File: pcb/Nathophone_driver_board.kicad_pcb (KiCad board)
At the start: 4 copper layers, 160 x 110 mm, 223 parts, among them J1 PJ-063AH, J10 TERM BLOCK, J11 54202-S0806ALF, J12 54202-S0806ALF, J13 54202-S0806ALF, J14 54202-S0806ALF, J3 Conn_01x30, J4 54202-S0806ALF, J5 TERM BLOCK, J6 TERM BLOCK, J7 TERM BLOCK, J8 TERM BLOCK, J9 TERM BLOCK, Q1 2N7002H, Q10 BSS84, Q11 BSS84, Q12 2N7002H, Q13 2N7002H, Q2 2N7002H, Q3 FDN340P, Q4 FQD11P06TM, Q5 FDN340P, Q6 BSS84, Q7 BSS84, Q8 BSS84, Q9 BSS84, SW1 1-1571986-1, SW2 PTS645SM43SMTR92 LFS, SW3 DS04-254-2-01BK-SMT, U1 LT8650SEV_PBF, U10 74LVC2G07, U2 SPX3819M5-L-3-3, U3 TAS5720MRSMR, U4 TAS5720MRSMR, U5 TAS5720MRSMR, U6 TAS5720MRSMR, U7 TAS5720MRSMR, U8 TAS5720MRSMR

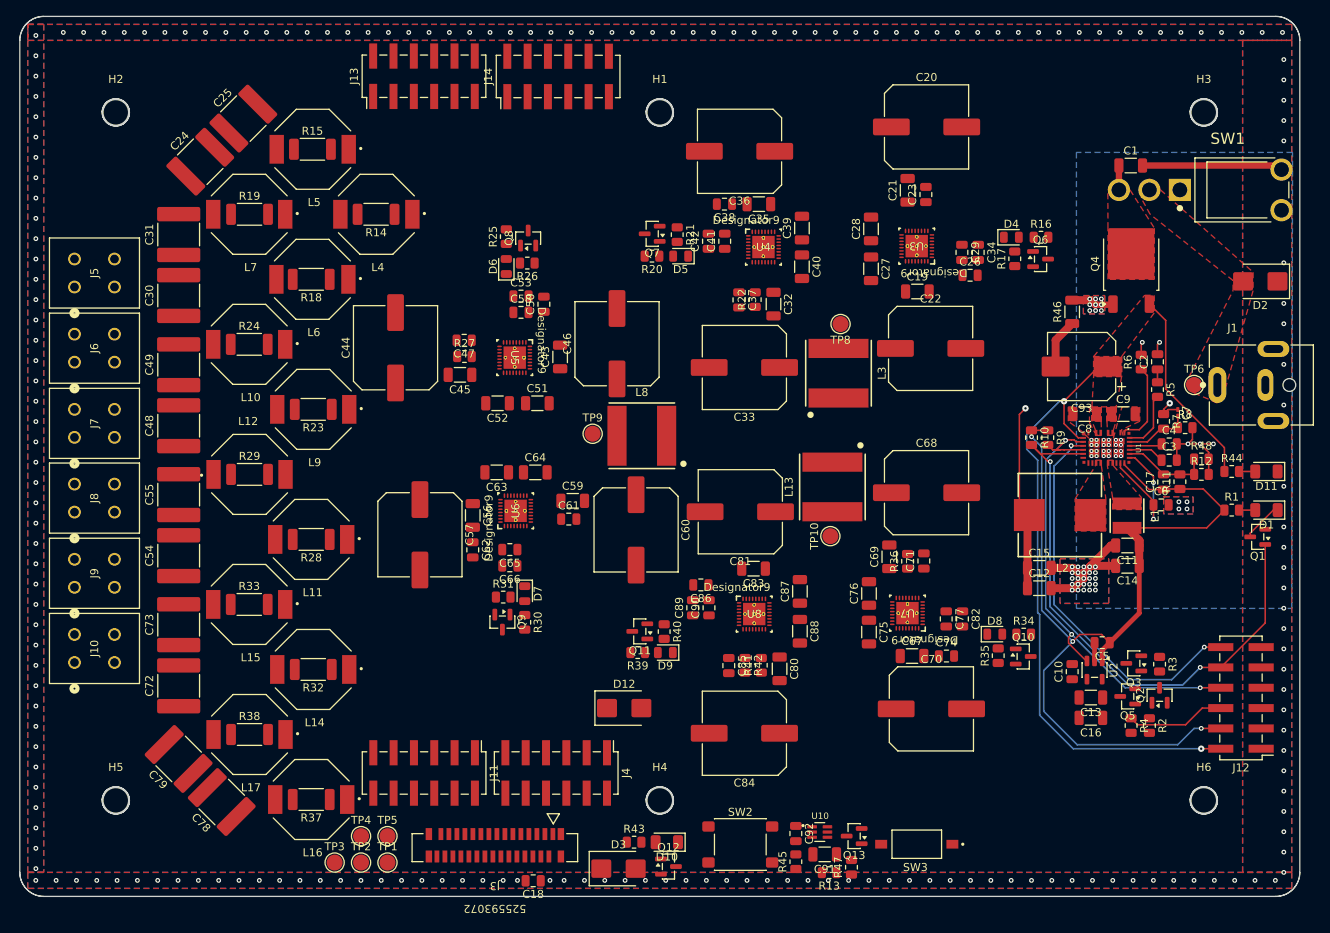
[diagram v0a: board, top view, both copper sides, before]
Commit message: ADDED Grounding Structure
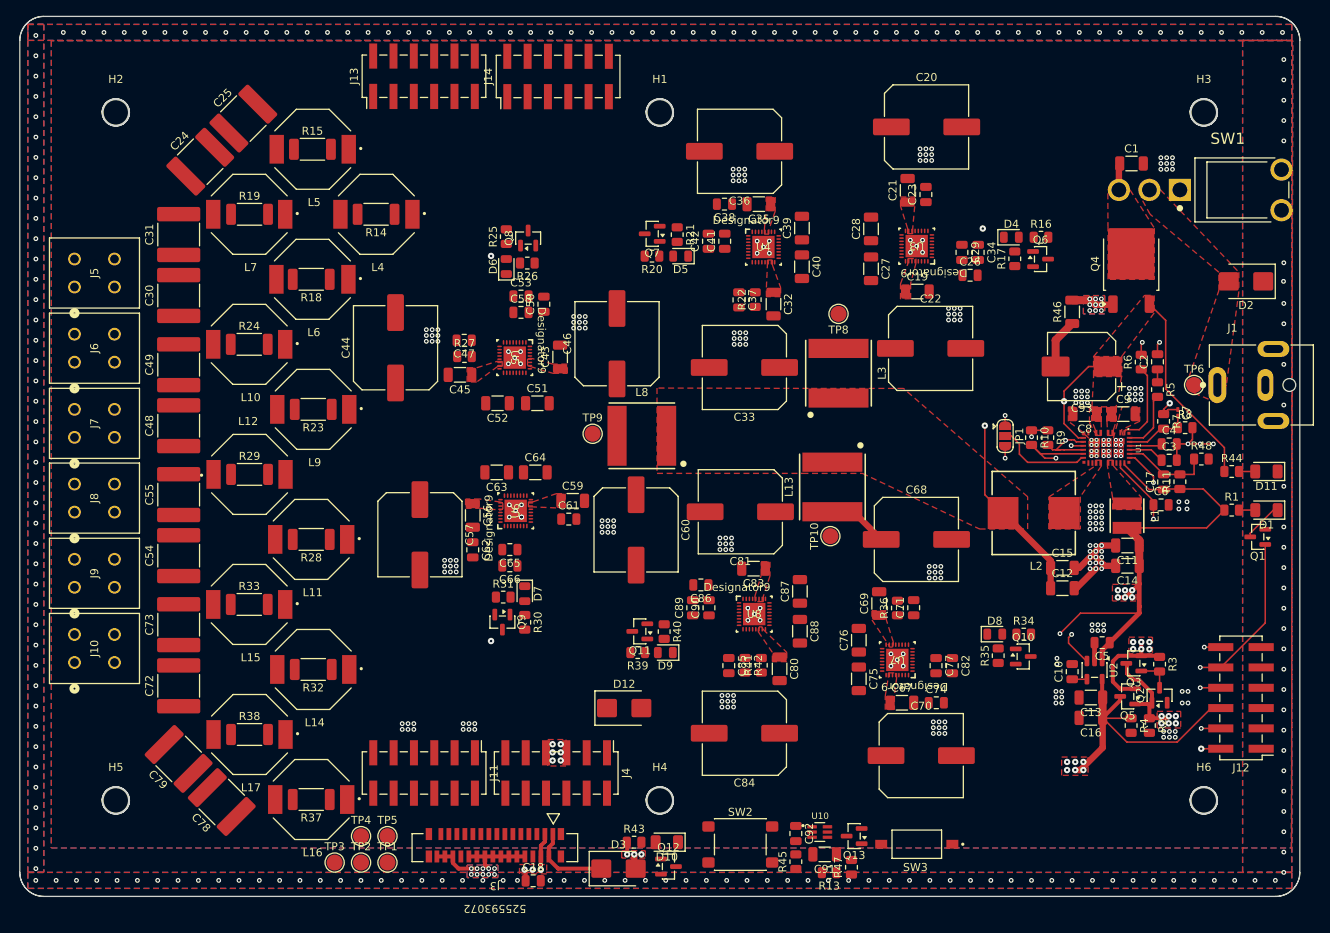
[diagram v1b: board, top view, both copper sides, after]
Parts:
- removed R12: 191k, Resistor_SMD:R_0805_2012Metric
- added JP1: Mode Selector, Jumper:SolderJumper-3_P1.3mm_Open_RoundedPad1.0x1.5mm, F.Cu at (185.2, 90.5)
- U3, U4, U5, U6, U7, U8: footprint symbols_footprints:VQFN32_RSM0032B -> symbols_footprints:VQFN32_RSM0032B_NV
- moved C67 5.98 mm to (172.3, 123.8)
- moved C74 5.98 mm to (176.6, 123.8)
- moved C68 5.98 mm to (174.1, 103.4)
- moved C70 5.98 mm to (174.7, 130.4)
- moved C71 5.98 mm to (173.7, 111.9)
- moved C75 5.98 mm to (166.9, 120.8)
- moved C76 5.98 mm to (166.9, 116.0)
- moved C77 5.98 mm to (176.5, 119.2)
- moved U7 5.98 mm to (171.7, 118.4)
- moved C69 5.98 mm to (169.4, 111.4)
- moved C82 5.98 mm to (178.6, 119.2)
- moved R36 5.98 mm to (171.7, 112.0)
- moved L2 3.28 mm to (188.7, 100.1)
- moved C12 2.89 mm to (192.3, 109.5)
- moved C15 2.89 mm to (192.3, 106.9)
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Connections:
- net Net-(U1-VC1) renamed VCC_REG
- U1 pad 16: unconnected-(U1-SYNC-Pad16) -> Net-(JP1-C)
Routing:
- net +3.3V: track 0.00 -> 206.3 mm, vias 0 -> 9
- net +3.3V_ext: track 0.00 -> 106.0 mm, vias 0 -> 9
- net +3.3V_int: track 12.4 -> 113.7 mm, vias 0 -> 12
- net +5.3V: track 118.3 -> 209.9 mm, vias 3 -> 12
- net VCC_REG: track 18.0 -> 39.3 mm, vias 2 -> 3
- net Net-(JP1-C): track 0.00 -> 12.1 mm
- net GND: track 60.5 -> 49.5 mm, vias 261 -> 480
- net +5V_ext: track 0.00 -> 10.4 mm
- net Net-(U7-AVDD): track 0.00 -> 7.53 mm
- net +15V: track 45.4 -> 51.7 mm
- net Net-(Q2-D): track 0.00 -> 4.35 mm
- net U1_temp: track 49.7 -> 47.5 mm
- net Net-(U2-BP): track 0.00 -> 1.85 mm
- net Net-(U3-AVDD): track 0.00 -> 1.11 mm
- net PG_2: track 72.3 -> 71.6 mm
- added copper zone on F.Cu, net +15V
- added copper zone on F.Cu, net +3.3V
- added copper zone on In1.Cu, net +3.3V
- added copper zone on F.Cu, net +3.3V_ext
- added copper zone on In1.Cu, net +3.3V_ext
- added copper zone on F.Cu, net +3.3V_int
- added copper zone on In1.Cu, net +3.3V_int
- added copper zone on F.Cu, net +5.3V
- added copper zone on In1.Cu, net +5.3V
- added copper zone on F.Cu, net Net-(U3-AVDD)
- added copper zone on F.Cu, net Net-(U5-AVDD)
- added copper zone on F.Cu, net Net-(U7-AVDD)

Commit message: DONE Routing first two drivers
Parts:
- moved C41 0.51 mm to (149.6, 66.0)
- moved C42 0.51 mm to (147.6, 66.0)
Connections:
- C51 pad 2: OUT1_P -> OUT3_P
- C52 pad 2: OUT1_N -> OUT3_N
- C63 pad 2: OUT2_P -> OUT4_P
- C64 pad 2: OUT2_N -> OUT4_N
- C75 pad 2: OUT1_P -> OUT5_P
- C76 pad 2: OUT1_N -> OUT5_N
- C87 pad 2: OUT2_P -> OUT6_P
- C88 pad 2: OUT2_N -> OUT6_N
- J14 pad 10: ~{FAULT_4} -> ~{FAULT_1}
- J14 pad 12: ~{FAULT_5} -> ~{FAULT_0}
- J14 pad 2: ~{FAULT_0} -> ~{FAULT_5}
- J14 pad 4: ~{FAULT_1} -> ~{FAULT_4}
- J14 pad 6: ~{FAULT_2} -> ~{FAULT_3}
- J14 pad 8: ~{FAULT_3} -> ~{FAULT_2}
- U5 pad 16: OUT1_N -> OUT3_N
- U5 pad 17: OUT1_N -> OUT3_N
- U5 pad 24: OUT1_P -> OUT3_P
- U5 pad 25: OUT1_P -> OUT3_P
- U6 pad 16: OUT2_N -> OUT4_N
- U6 pad 17: OUT2_N -> OUT4_N
- U6 pad 24: OUT2_P -> OUT4_P
- U6 pad 25: OUT2_P -> OUT4_P
- U7 pad 16: OUT1_N -> OUT5_N
- U7 pad 17: OUT1_N -> OUT5_N
- U7 pad 24: OUT1_P -> OUT5_P
- U7 pad 25: OUT1_P -> OUT5_P
- U8 pad 16: OUT2_N -> OUT6_N
- U8 pad 17: OUT2_N -> OUT6_N
- U8 pad 24: OUT2_P -> OUT6_P
- U8 pad 25: OUT2_P -> OUT6_P
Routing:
- net OUT2_N: track 0.00 -> 110.2 mm, vias 0 -> 9
- net OUT2_P: track 0.00 -> 97.9 mm, vias 0 -> 6
- net OUT1_P: track 0.00 -> 97.1 mm, vias 0 -> 10
- net Net-(U3-AVDD): track 1.11 -> 96.6 mm
- net OUT1_N: track 0.00 -> 85.2 mm, vias 0 -> 6
- net ~{FAULT_0}: track 0.00 -> 80.5 mm, vias 0 -> 2
- net +3.3V: track 206.3 -> 262.2 mm, vias 9 -> 11
- net Net-(U5-AVDD): track 0.00 -> 51.4 mm
- net OUT3_P: track 0.00 -> 46.8 mm, vias 0 -> 2
- net Net-(U7-AVDD): track 7.53 -> 50.7 mm
- net ~{FAULT_1}: track 0.00 -> 42.8 mm
- net ~{Group_SDZ}: track 0.00 -> 41.3 mm, vias 0 -> 2
- net SDA: track 0.00 -> 41.3 mm, vias 0 -> 2
- net SCL: track 0.00 -> 40.2 mm, vias 0 -> 2
- net SCLK: track 0.00 -> 39.7 mm, vias 0 -> 2
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- added copper zone on F.Cu, net OUT1_N
- added copper zone on F.Cu, net OUT1_P
- added copper zone on F.Cu, net OUT2_N
- added copper zone on F.Cu, net OUT2_P

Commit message: DONE Digital Routing
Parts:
- moved D10 12.5 mm to (154.9, 137.9)
- moved Q12 12.5 mm to (155.1, 141.0)
- moved R43 12.5 mm to (150.8, 137.9)
- moved D3 12.5 mm to (148.9, 141.2)
- moved C91 12.3 mm to (173.5, 137.2)
- moved SW3 12.2 mm to (185.7, 137.4), turned to -90 degrees
- moved Q13 11.8 mm to (178.0, 139.2)
- moved R45 11.2 mm to (170.1, 141.8)
- moved C92 11.2 mm to (170.1, 138.3)
- moved SW2 11.2 mm to (163.1, 139.7)
- moved U10 11.2 mm to (173.2, 139.7)
- moved R13 10.4 mm to (173.1, 142.0), turned to 0 degrees
- moved R47 10.4 mm to (176.0, 141.9)
- moved D12 6.22 mm to (141.5, 129.3)
- moved J10 6.17 mm to (68.8, 118.9), turned to -90 degrees
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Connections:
- C24 pad 1: Net-(J5-Pin_1) -> Net-(J5-Pin_3)
- C25 pad 2: Net-(J5-Pin_3) -> Net-(J5-Pin_1)
- C30 pad 1: Net-(J6-Pin_1) -> Net-(J6-Pin_3)
- C31 pad 2: Net-(J6-Pin_3) -> Net-(J6-Pin_1)
- C48 pad 1: Net-(J7-Pin_1) -> Net-(J7-Pin_3)
- C49 pad 2: Net-(J7-Pin_3) -> Net-(J7-Pin_1)
- C54 pad 1: Net-(J8-Pin_1) -> Net-(J8-Pin_3)
- C55 pad 2: Net-(J8-Pin_3) -> Net-(J8-Pin_1)
- C72 pad 1: Net-(J9-Pin_1) -> Net-(J9-Pin_3)
- C73 pad 2: Net-(J9-Pin_3) -> Net-(J9-Pin_1)
- C78 pad 1: Net-(J10-Pin_1) -> Net-(J10-Pin_3)
- C79 pad 2: Net-(J10-Pin_3) -> Net-(J10-Pin_1)
- L10 pad 2: Net-(J7-Pin_3) -> Net-(J7-Pin_1)
- L11 pad 2: Net-(J8-Pin_1) -> Net-(J8-Pin_3)
- L12 pad 2: Net-(J8-Pin_3) -> Net-(J8-Pin_1)
- L14 pad 2: Net-(J9-Pin_1) -> Net-(J9-Pin_3)
- L15 pad 2: Net-(J9-Pin_3) -> Net-(J9-Pin_1)
- L16 pad 2: Net-(J10-Pin_1) -> Net-(J10-Pin_3)
- L17 pad 2: Net-(J10-Pin_3) -> Net-(J10-Pin_1)
- L4 pad 2: Net-(J5-Pin_1) -> Net-(J5-Pin_3)
- L5 pad 2: Net-(J5-Pin_3) -> Net-(J5-Pin_1)
- L6 pad 2: Net-(J6-Pin_1) -> Net-(J6-Pin_3)
- L7 pad 2: Net-(J6-Pin_3) -> Net-(J6-Pin_1)
- L9 pad 2: Net-(J7-Pin_1) -> Net-(J7-Pin_3)
- R14 pad 2: Net-(J5-Pin_1) -> Net-(J5-Pin_3)
- R15 pad 1: Net-(J5-Pin_3) -> Net-(J5-Pin_1)
- R18 pad 2: Net-(J6-Pin_1) -> Net-(J6-Pin_3)
- R19 pad 1: Net-(J6-Pin_3) -> Net-(J6-Pin_1)
- R23 pad 2: Net-(J7-Pin_1) -> Net-(J7-Pin_3)
- R24 pad 1: Net-(J7-Pin_3) -> Net-(J7-Pin_1)
- R28 pad 2: Net-(J8-Pin_1) -> Net-(J8-Pin_3)
- R29 pad 1: Net-(J8-Pin_3) -> Net-(J8-Pin_1)
- R32 pad 2: Net-(J9-Pin_1) -> Net-(J9-Pin_3)
- R33 pad 1: Net-(J9-Pin_3) -> Net-(J9-Pin_1)
- R37 pad 2: Net-(J10-Pin_1) -> Net-(J10-Pin_3)
- R38 pad 1: Net-(J10-Pin_3) -> Net-(J10-Pin_1)
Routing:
- net LRCLK: track 39.7 -> 262.4 mm, vias 2 -> 7
- net MRCLK: track 39.2 -> 257.6 mm, vias 2 -> 7
- net SCLK: track 39.7 -> 247.5 mm, vias 2 -> 7
- net DATA: track 39.2 -> 239.4 mm, vias 2 -> 7
- net SDA: track 41.3 -> 234.6 mm, vias 2 -> 7
- net SCL: track 40.2 -> 231.3 mm, vias 2 -> 7
- net ~{Group_SDZ}: track 41.3 -> 226.9 mm, vias 2 -> 7
- net +3.3V: track 262.2 -> 419.9 mm, vias 11 -> 12
- net OUT5_N: track 0.00 -> 86.5 mm, vias 0 -> 6
- net OUT6_P: track 0.00 -> 78.1 mm, vias 0 -> 6
- net OUT6_N: track 0.00 -> 74.1 mm, vias 0 -> 6
- net OUT5_P: track 0.00 -> 73.1 mm, vias 0 -> 6
- net GND: track 88.5 -> 147.3 mm
- net ~{ADC_RST_N_OUT}: track 0.00 -> 53.6 mm, vias 0 -> 2
- net Net-(U5-AVDD): track 51.4 -> 94.0 mm
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- added copper zone on In2.Cu, net +3.3V_int
- added copper zone on F.Cu, net OUT3_N
- added copper zone on F.Cu, net OUT3_P
- added copper zone on F.Cu, net OUT4_N
- added copper zone on F.Cu, net OUT4_P
- added copper zone on F.Cu, net OUT5_N
- added copper zone on F.Cu, net OUT5_P
- added copper zone on F.Cu, net OUT6_N
- added copper zone on F.Cu, net OUT6_P

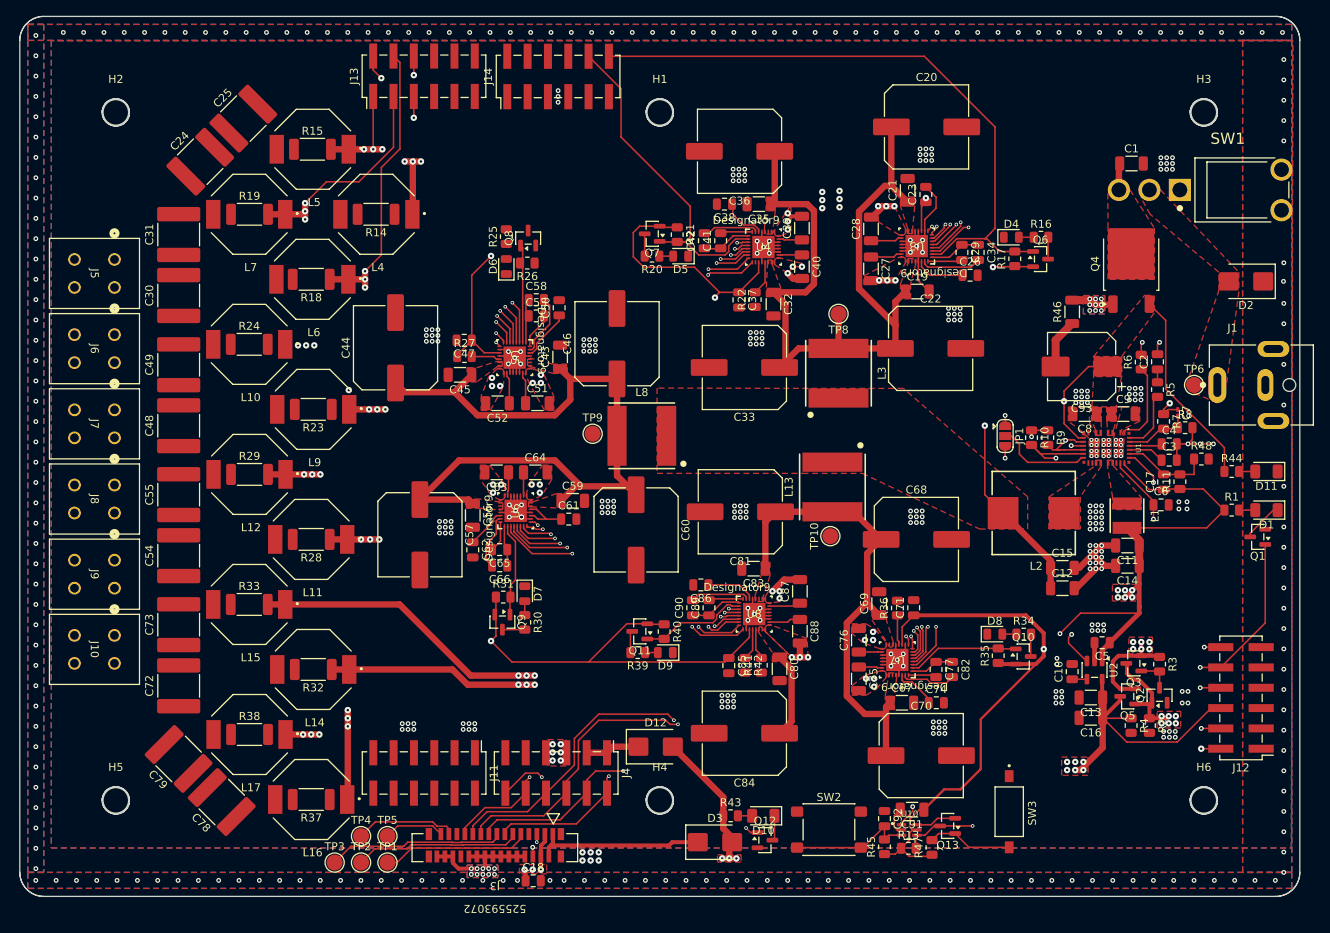
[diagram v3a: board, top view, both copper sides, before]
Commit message: COMPLETED Routing, DRC checked
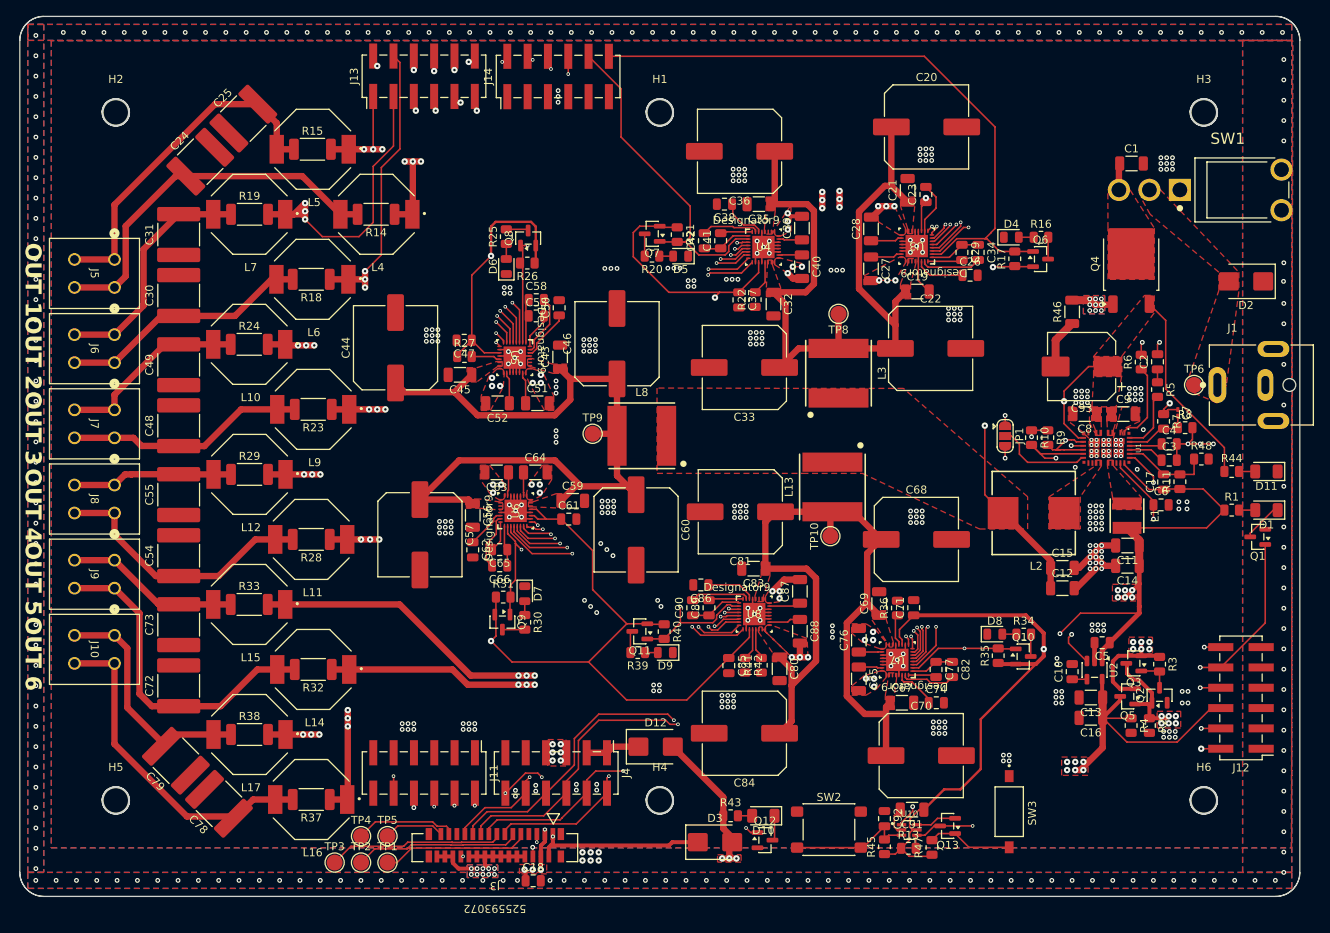
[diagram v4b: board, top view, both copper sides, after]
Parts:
- moved C79 0.41 mm to (81.5, 131.0)
- moved C78 0.41 mm to (86.9, 136.4)
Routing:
- net OUT6_N: track 74.1 -> 198.6 mm, vias 6 -> 7
- net ~{FAULT_4}: track 13.9 -> 138.1 mm, vias 0 -> 2
- net OUT6_P: track 78.1 -> 202.2 mm, vias 6 -> 7
- net ~{FAULT_5}: track 13.6 -> 109.7 mm, vias 0 -> 2
- net OUT5_P: track 73.1 -> 166.9 mm, vias 6 -> 7
- net OUT5_N: track 86.5 -> 174.7 mm, vias 6 -> 7
- net ~{FAULT_3}: track 11.8 -> 78.9 mm, vias 0 -> 2
- net OUT4_P: track 28.0 -> 90.6 mm, vias 6 -> 7
- net OUT4_N: track 38.0 -> 92.2 mm, vias 6 -> 7
- net Net-(J5-Pin_3): track 0.00 -> 46.8 mm
- net ~{Group_SDZ}: track 226.9 -> 272.8 mm, vias 7 -> 8
- net Net-(J5-Pin_1): track 0.00 -> 43.7 mm
- net Net-(J10-Pin_3): track 0.00 -> 42.0 mm
- net Net-(J9-Pin_3): track 0.00 -> 41.5 mm
- net +3.3V: track 419.9 -> 455.0 mm
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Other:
- board text added: "OUT 1"
- board text added: "OUT 2"
- board text added: "OUT 3"
- board text added: "OUT 4"
- board text added: "OUT 5"
- board text added: "OUT 6"

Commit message: CHANGED Output and Power Track widths to 1mm
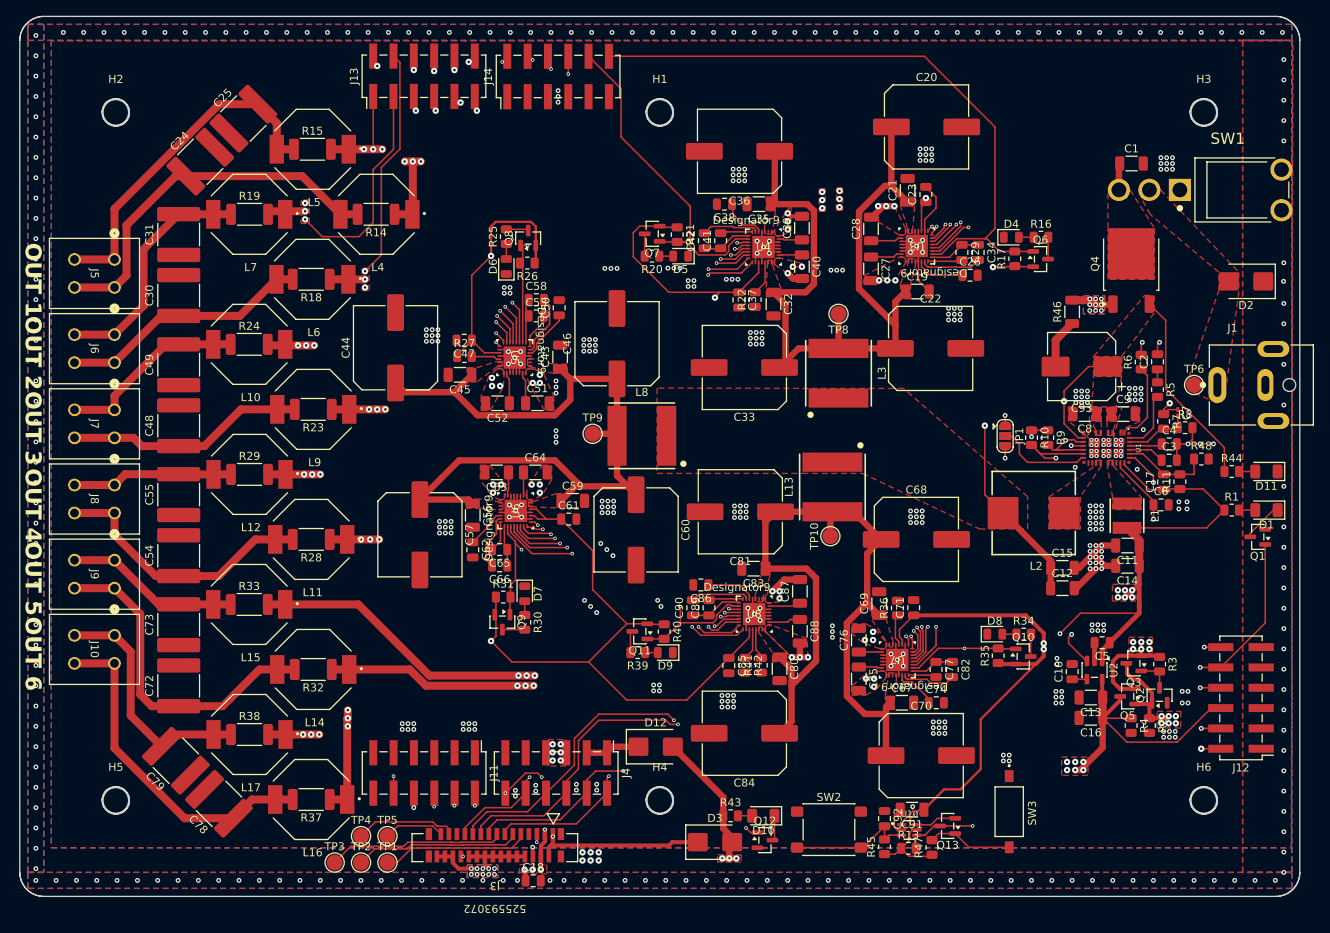
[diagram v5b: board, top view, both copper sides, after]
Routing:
- net OUT2_N: track 122.0 -> 116.0 mm
- net OUT6_N: track 198.6 -> 203.2 mm
- net +3.3V_ext: track 116.7 -> 120.7 mm
- net +3.3V_int: track 129.9 -> 133.0 mm
- net ~{Group_SDZ}: track 272.8 -> 270.0 mm
- net Net-(J10-Pin_1): track 30.1 -> 32.4 mm
- net OUT5_P: track 166.9 -> 168.3 mm
- net +3.3V: track 455.0 -> 456.1 mm, vias 12 -> 13
- net OUT5_N: track 174.7 -> 175.8 mm
- net OUT1_P: track 97.8 -> 97.0 mm
- net MRCLK: track 257.8 -> 257.2 mm
- added copper zone on In2.Cu, net OUT1_P
- added copper zone on In1.Cu, net OUT2_N
- added copper zone on In2.Cu, net OUT2_N
- added copper zone on In1.Cu, net OUT2_P
